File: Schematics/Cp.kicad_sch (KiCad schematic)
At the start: 42 parts, among them Q10 2SK30A, Q11 2SK30A, Q5 2SC1815, Q6 2SC1815, Q7 2SC1815, Q8 2SC1815, SW1 SW_DPDT_x2, U3 CA3080

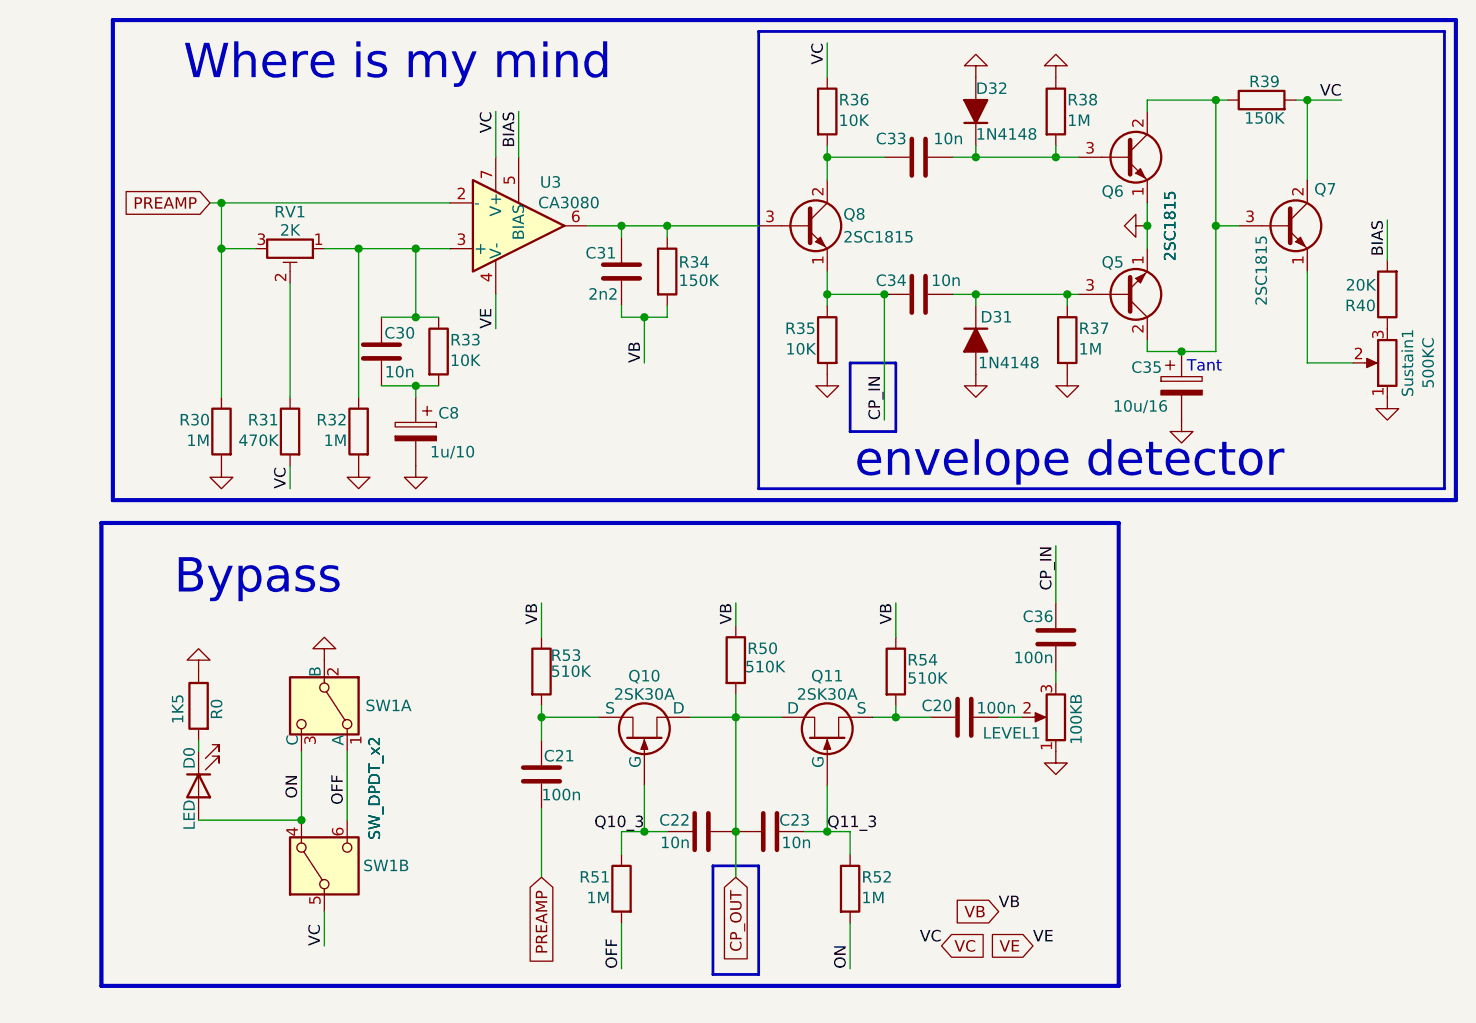
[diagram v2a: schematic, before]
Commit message: Big Upd
Schemaics: Tone Stack moved to differend file and made some differend variants of, reassigned some footprints

Readme upd: added tone stacks types
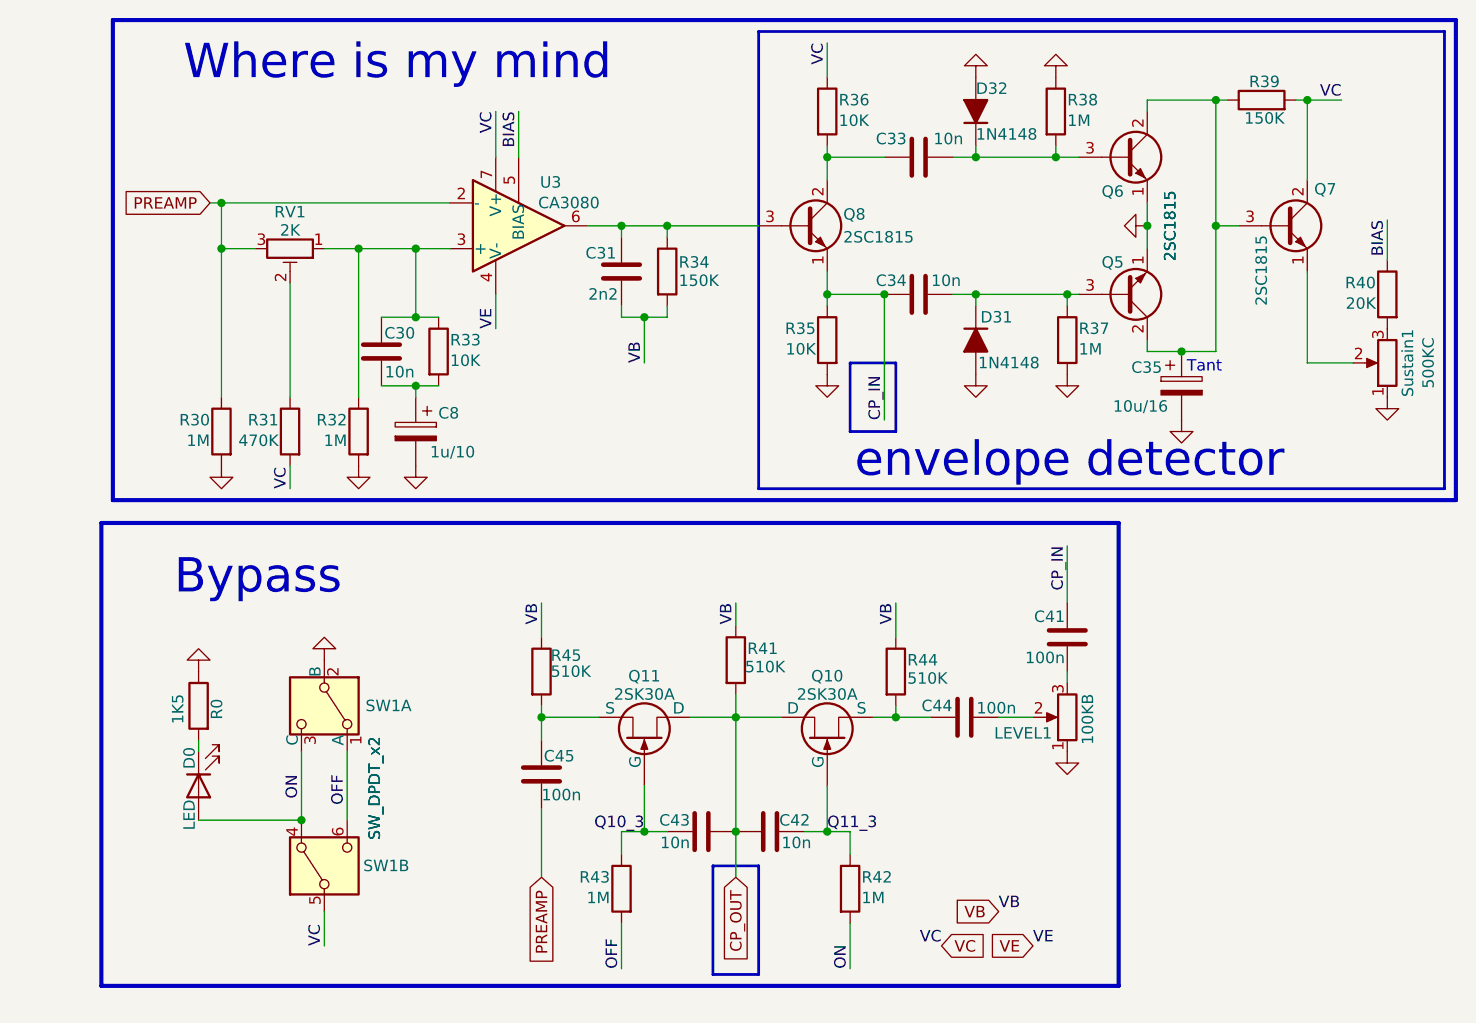
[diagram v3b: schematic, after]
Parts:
- Q5, Q6, Q7, Q8: footprint Package_TO_SOT_THT:TO-92_Inline -> Package_TO_SOT_THT:TO-92_Inline_Wide
- Sustain1: footprint Potentiometer_THT:Potentiometer_Bourns_3296W_Vertical -> PrLib:potentiometer
- renumbered C36 to C41, C23 to C42, C22 to C43, C20 to C44, C21 to C45, Q11 to Q10, Q10 to Q11, R50 to R41, R52 to R42, R51 to R43, R54 to R44, R53 to R45
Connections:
- net BIAS: now also R40.1; no longer R40.2
- net at Sustain1.3: now also R40.2; no longer R40.1
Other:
- moved on the sheet: C41, LEVEL1, R40
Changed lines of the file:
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@@
 	(wire
 		(pts
-			(xy 121.92 87.63) (xy 121.92 88.9)
+			(xy 123.19 87.63) (xy 123.19 88.9)
 		)
 		(stroke
@@
 	(wire
 		(pts
-			(xy 121.92 73.66) (xy 121.92 80.01)
+			(xy 123.19 73.66) (xy 123.19 80.01)
 		)
 		(stroke
@@
 	(wire
 		(pts
-			(xy 115.57 92.71) (xy 118.11 92.71)
+			(xy 115.57 92.71) (xy 119.38 92.71)
 		)
 		(stroke
@@
 	)
 	(label "CP_IN"
-		(at 121.92 73.66 270)
+		(at 123.19 73.66 270)
 		(effects
 			(font
@@
 			)
 		)
-		(property "Footprint" "Package_TO_SOT_THT:TO-92_Inline"
+		(property "Footprint" "Package_TO_SOT_THT:TO-92_Inline_Wide"
 			(at 134.62 32.385 0)
 			(hide yes)
@@
 		(in_pos_files yes)
 		(dnp no)
-		(property "Reference" "C20"
+		(property "Reference" "C44"
 			(at 108.712 91.44 90)
 			(show_name no)
@@
 			(project "AMP-MA"
 				(path "/4094031b-a9da-4ac5-aaa1-42b342c92a3e/d432553b-ab0c-45ec-bbdd-5af2e9267855"
-					(reference "C20")
+					(reference "C44")
 					(unit 1)
 				)
@@
 			)
 		)
-		(property "Footprint" "Potentiometer_THT:Potentiometer_Bourns_3296W_Vertical"
+		(property "Footprint" "PrLib:potentiometer"
 			(at 158.75 53.34 0)
 			(hide yes)
@@
 	(symbol
 		(lib_id "Device:R_Potentiometer")
-		(at 121.92 92.71 180)
+		(at 123.19 92.71 180)
 		(unit 1)
 		(body_style 1)
@@
 		(dnp no)
 		(property "Reference" "LEVEL1"
-			(at 113.792 94.488 0)
+			(at 115.062 94.488 0)
 			(show_name no)
 			(do_not_autoplace yes)
@@
 		)
 		(property "Value" "100KB"
-			(at 124.206 95.758 90)
+			(at 125.476 95.758 90)
 			(show_name no)
 			(do_not_autoplace no)
@@
 		)
 		(property "Footprint" "PrLib:potentiometer"
-			(at 121.92 92.71 0)
+			(at 123.19 92.71 0)
 			(hide yes)
 			(show_name no)
@@
 		)
 		(property "Datasheet" ""
-			(at 121.92 92.71 0)
+			(at 123.19 92.71 0)
 			(hide yes)
 			(show_name no)
@@
 		)
 		(property "Description" "Potentiometer"
-			(at 121.92 92.71 0)
+			(at 123.19 92.71 0)
 			(hide yes)
 			(show_name no)
@@
 		)
 		(property "Sim.Device" "R"
-			(at 121.92 92.71 0)
+			(at 123.19 92.71 0)
 			(hide yes)
 			(show_name no)
@@
 		)
 		(property "Sim.Type" "POT"
-			(at 121.92 92.71 0)
+			(at 123.19 92.71 0)
 			(hide yes)
 			(show_name no)
@@
 		)
 		(property "Sim.Pins" "1=r0 2=wiper 3=r1"
-			(at 121.92 92.71 0)
+			(at 123.19 92.71 0)
 			(hide yes)
 			(show_name no)
@@
 			)
 		)
-		(property "Footprint" "Package_TO_SOT_THT:TO-92_Inline"
+		(property "Footprint" "Package_TO_SOT_THT:TO-92_Inline_Wide"
 			(at 99.06 40.005 0)
 			(hide yes)
@@
 		(in_pos_files yes)
 		(dnp no)
-		(property "Reference" "C22"
+		(property "Reference" "C43"
 			(at 81.28 104.902 90)
 			(show_name no)
@@
 			(project "AMP-MA"
 				(path "/4094031b-a9da-4ac5-aaa1-42b342c92a3e/d432553b-ab0c-45ec-bbdd-5af2e9267855"
-					(reference "C22")
+					(reference "C43")
 					(unit 1)
 				)
@@
 		(in_pos_files yes)
 		(dnp no)
-		(property "Reference" "C21"
+		(property "Reference" "C45"
 			(at 65.024 97.028 0)
 			(show_name no)
@@
 			(project "AMP-MA"
 				(path "/4094031b-a9da-4ac5-aaa1-42b342c92a3e/d432553b-ab0c-45ec-bbdd-5af2e9267855"
-					(reference "C21")
+					(reference "C45")
 					(unit 1)
 				)
@@
 		(in_pos_files yes)
 		(dnp no)
-		(property "Reference" "R50"
+		(property "Reference" "R41"
 			(at 87.63 85.09 0)
 			(show_name no)
@@
 			(project "AMP-MA"
 				(path "/4094031b-a9da-4ac5-aaa1-42b342c92a3e/d432553b-ab0c-45ec-bbdd-5af2e9267855"
-					(reference "R50")
+					(reference "R41")
 					(unit 1)
 				)
@@
 		(in_pos_files yes)
 		(dnp no)
-		(property "Reference" "R54"
+		(property "Reference" "R44"
 			(at 105.41 86.36 0)
 			(show_name no)
@@
 			(project "AMP-MA"
 				(path "/4094031b-a9da-4ac5-aaa1-42b342c92a3e/d432553b-ab0c-45ec-bbdd-5af2e9267855"
-					(reference "R54")
+					(reference "R44")
 					(unit 1)
 				)
@@
 	(symbol
 		(lib_id "Device:C")
-		(at 121.92 83.82 180)
+		(at 123.19 83.82 180)
 		(unit 1)
 		(body_style 1)
@@
 		(in_pos_files yes)
 		(dnp no)
-		(property "Reference" "C36"
-			(at 121.666 81.534 0)
+		(property "Reference" "C41"
+			(at 122.936 81.534 0)
 			(show_name no)
 			(do_not_autoplace no)
@@
 		)
 		(property "Value" "100n"
-			(at 121.666 86.106 0)
+			(at 122.936 86.106 0)
 			(show_name no)
 			(do_not_autoplace no)
@@
 		)
 		(property "Footprint" "PrLib:C_disc_D7_W2.5_P5"
-			(at 120.9548 80.01 0)
+			(at 122.2248 80.01 0)
 			(hide yes)
 			(show_name no)
@@
 		)
 		(property "Datasheet" ""
-			(at 121.92 83.82 0)
+			(at 123.19 83.82 0)
 			(hide yes)
 			(show_name no)
@@
 		)
 		(property "Description" "Unpolarized capacitor"
-			(at 121.92 83.82 0)
+			(at 123.19 83.82 0)
 			(hide yes)
 			(show_name no)
@@
 			(project "AMP-MA"
 				(path "/4094031b-a9da-4ac5-aaa1-42b342c92a3e/d432553b-ab0c-45ec-bbdd-5af2e9267855"
-					(reference "C36")
+					(reference "C41")
 					(unit 1)
 				)
@@
 	(symbol
 		(lib_id "power:GND")
-		(at 121.92 96.52 0)
+		(at 123.19 96.52 0)
 		(mirror y)
 		(unit 1)
@@
 		(fields_autoplaced yes)
 		(property "Reference" "#PWR031"
-			(at 121.92 102.87 0)
+			(at 123.19 102.87 0)
 			(hide yes)
 			(show_name no)
@@
 		)
 		(property "Value" "GND"
-			(at 121.92 101.6 0)
+			(at 123.19 101.6 0)
 			(hide yes)
 			(show_name no)
@@
 		)
 		(property "Footprint" ""
-			(at 121.92 96.52 0)
+			(at 123.19 96.52 0)
 			(hide yes)
 			(show_name no)
@@
 		)
 		(property "Datasheet" ""
-			(at 121.92 96.52 0)
+			(at 123.19 96.52 0)
 			(hide yes)
 			(show_name no)
@@
 		)
 		(property "Description" "Power symbol creates a global label with name \"GND\" , ground"
-			(at 121.92 96.52 0)
+			(at 123.19 96.52 0)
 			(hide yes)
 			(show_name no)
@@
 			)
 		)
-		(property "Footprint" "Package_TO_SOT_THT:TO-92_Inline"
+		(property "Footprint" "Package_TO_SOT_THT:TO-92_Inline_Wide"
 			(at 152.4 40.005 0)
 			(hide yes)
@@
 		(in_pos_files yes)
 		(dnp no)
-		(property "Reference" "R52"
+		(property "Reference" "R42"
 			(at 100.33 110.49 0)
 			(show_name no)
@@
 			(project "AMP-MA"
 				(path "/4094031b-a9da-4ac5-aaa1-42b342c92a3e/d432553b-ab0c-45ec-bbdd-5af2e9267855"
-					(reference "R52")
+					(reference "R42")
 					(unit 1)
 				)
@@
 		(in_pos_files yes)
 		(dnp no)
-		(property "Reference" "Q11"
+		(property "Reference" "Q10"
 			(at 96.52 88.138 90)
 			(show_name no)
@@
 			(project "AMP-MA"
 				(path "/4094031b-a9da-4ac5-aaa1-42b342c92a3e/d432553b-ab0c-45ec-bbdd-5af2e9267855"
-					(reference "Q11")
+					(reference "Q10")
 					(unit 1)
 				)
@@
 			)
 		)
-		(property "Footprint" "Package_TO_SOT_THT:TO-92_Inline"
+		(property "Footprint" "Package_TO_SOT_THT:TO-92_Inline_Wide"
 			(at 134.62 43.815 0)
 			(hide yes)
@@
 		(in_pos_files yes)
 		(dnp no)
-		(property "Reference" "R53"
+		(property "Reference" "R45"
 			(at 65.786 85.852 0)
 			(show_name no)
@@
 			(project "AMP-MA"
 				(path "/4094031b-a9da-4ac5-aaa1-42b342c92a3e/d432553b-ab0c-45ec-bbdd-5af2e9267855"
-					(reference "R53")
+					(reference "R45")
 					(unit 1)
 				)
@@
 		(in_pos_files yes)
 		(dnp no)
-		(property "Reference" "R51"
+		(property "Reference" "R43"
 			(at 72.39 110.49 0)
 			(show_name no)
@@
 			(project "AMP-MA"
 				(path "/4094031b-a9da-4ac5-aaa1-42b342c92a3e/d432553b-ab0c-45ec-bbdd-5af2e9267855"
-					(reference "R51")
+					(reference "R43")
 					(unit 1)
 				)
@@
 	(symbol
 		(lib_id "Device:R")
-		(at 158.75 45.72 180)
+		(at 158.75 45.72 0)
+		(mirror y)
 		(unit 1)
 		(body_style 1)
@@
 		(dnp no)
 		(property "Reference" "R40"
-			(at 157.48 46.99 0)
+			(at 157.48 44.45 0)
 			(show_name no)
 			(do_not_autoplace no)
@@
 		)
 		(property "Value" "20K"
-			(at 157.48 44.704 0)
+			(at 157.48 46.736 0)
 			(show_name no)
 			(do_not_autoplace no)
@@
 		(in_pos_files yes)
 		(dnp no)
-		(property "Reference" "C23"
+		(property "Reference" "C42"
 			(at 91.186 104.902 90)
 			(show_name no)
@@
 			(project "AMP-MA"
 				(path "/4094031b-a9da-4ac5-aaa1-42b342c92a3e/d432553b-ab0c-45ec-bbdd-5af2e9267855"
-					(reference "C23")
+					(reference "C42")
 					(unit 1)
 				)
@@
 		(in_pos_files yes)
 		(dnp no)
-		(property "Reference" "Q10"
+		(property "Reference" "Q11"
 			(at 76.2 88.138 90)
 			(show_name no)
@@
 			(project "AMP-MA"
 				(path "/4094031b-a9da-4ac5-aaa1-42b342c92a3e/d432553b-ab0c-45ec-bbdd-5af2e9267855"
-					(reference "Q10")
+					(reference "Q11")
 					(unit 1)
 				)

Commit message: Cosmetic upd
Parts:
- C8: value 1u/10 -> 1u
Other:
- moved on the sheet: C30, C33, C34, C35, C41, C42, C43, C44, C45, C8, D0, D31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

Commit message: Version 0.1.0 Pre-Release
Reworked PCB, reanotated some components, changed some footprints
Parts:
- C35: footprint PrLib:C_disc_D7_W2.5_P5 -> Capacitor_THT:CP_Radial_Tantal_D5.5mm_P2.50mm
- LEVEL1: footprint PrLib:potentiometer -> Potentiometer_THT:Potentiometer_Bourns_3296W_Vertical
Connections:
- net CP_OUT renamed BP_OUT
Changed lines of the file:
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@@
 		)
 	)
-	(global_label "CP_OUT"
+	(global_label "BP_OUT"
 		(shape input)
 		(at 80.01 110.49 270)
@@
 		)
 		(property "Intersheetrefs" "${INTERSHEET_REFS}"
-			(at 80.01 120.6114 90)
+			(at 80.01 120.361 90)
 			(hide yes)
 			(show_name no)
@@
 			)
 		)
-		(property "Footprint" "PrLib:potentiometer"
+		(property "Footprint" "Potentiometer_THT:Potentiometer_Bourns_3296W_Vertical"
 			(at 116.84 92.71 0)
 			(hide yes)
@@
 		(dnp no)
 		(property "Reference" "Q8"
-			(at 95.758 36.83 0)
+			(at 96.012 36.83 0)
 			(show_name no)
 			(do_not_autoplace no)
@@
 		(dnp no)
 		(property "Reference" "Q7"
-			(at 149.352 34.036 0)
+			(at 143.002 34.544 0)
 			(show_name no)
 			(do_not_autoplace no)
@@
 		)
 		(property "Value" "2SC1815"
-			(at 143.51 46.99 90)
+			(at 151.384 38.1 90)
 			(show_name no)
 			(do_not_autoplace no)
@@
 					(size 1.27 1.27)
 				)
-				(justify left)
 			)
 		)
@@
 			)
 		)
-		(property "Footprint" "PrLib:C_disc_D7_W2.5_P5"
+		(property "Footprint" "Capacitor_THT:CP_Radial_Tantal_D5.5mm_P2.50mm"
 			(at 133.6548 59.69 0)
 			(hide yes)
